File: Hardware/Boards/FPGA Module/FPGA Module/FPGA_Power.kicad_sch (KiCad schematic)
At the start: 41 parts, among them U1 XCKU3P-FFVA676

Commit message: Added NC to unused pins
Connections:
- no-connect marks 0 -> 1
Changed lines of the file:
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@@
 		(color 0 0 0 0)
 	)
+	(no_connect
+		(at 373.38 228.6)
+	)
 	(wire
 		(pts
@@
 	(wire
 		(pts
-			(xy 220.98 96.52) (xy 224.79 96.52)
-		)
-		(stroke
-			(width 0)
-			(type default)
-		)
-	)
-	(wire
-		(pts
 			(xy 374.65 175.26) (xy 373.38 175.26)
 		)
@@
 	(wire
 		(pts
+			(xy 220.98 109.22) (xy 224.79 109.22)
+		)
+		(stroke
+			(width 0)
+			(type default)
+		)
+	)
+	(wire
+		(pts
 			(xy 354.33 228.6) (xy 354.33 234.95)
 		)
@@
 	(wire
 		(pts
+			(xy 220.98 96.52) (xy 224.79 96.52)
+		)
+		(stroke
+			(width 0)
+			(type default)
+		)
+	)
+	(wire
+		(pts
 			(xy 212.09 134.62) (xy 213.36 134.62)
 		)
@@
 		)
 		(stroke
-			(width 0)
-			(type default)
-		)
-	)
-	(wire
-		(pts
-			(xy 220.98 109.22) (xy 224.79 109.22)
-		)
-		(stroke

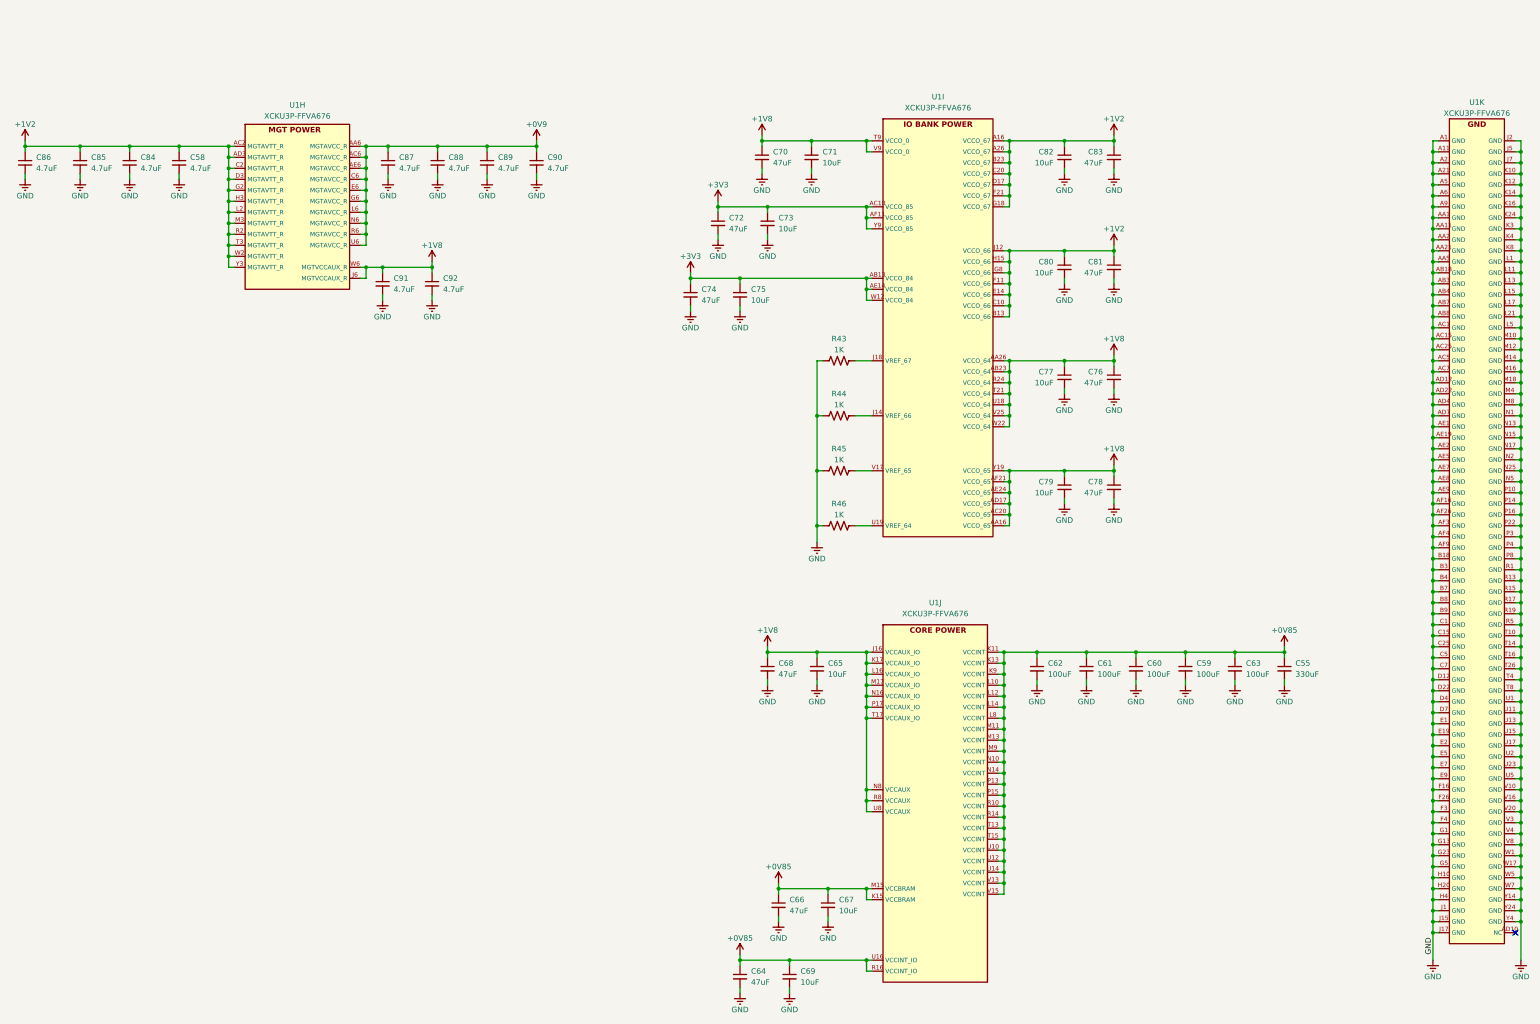
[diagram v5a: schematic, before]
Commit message: Completed FPGA module PCB layout
Started PCB routing
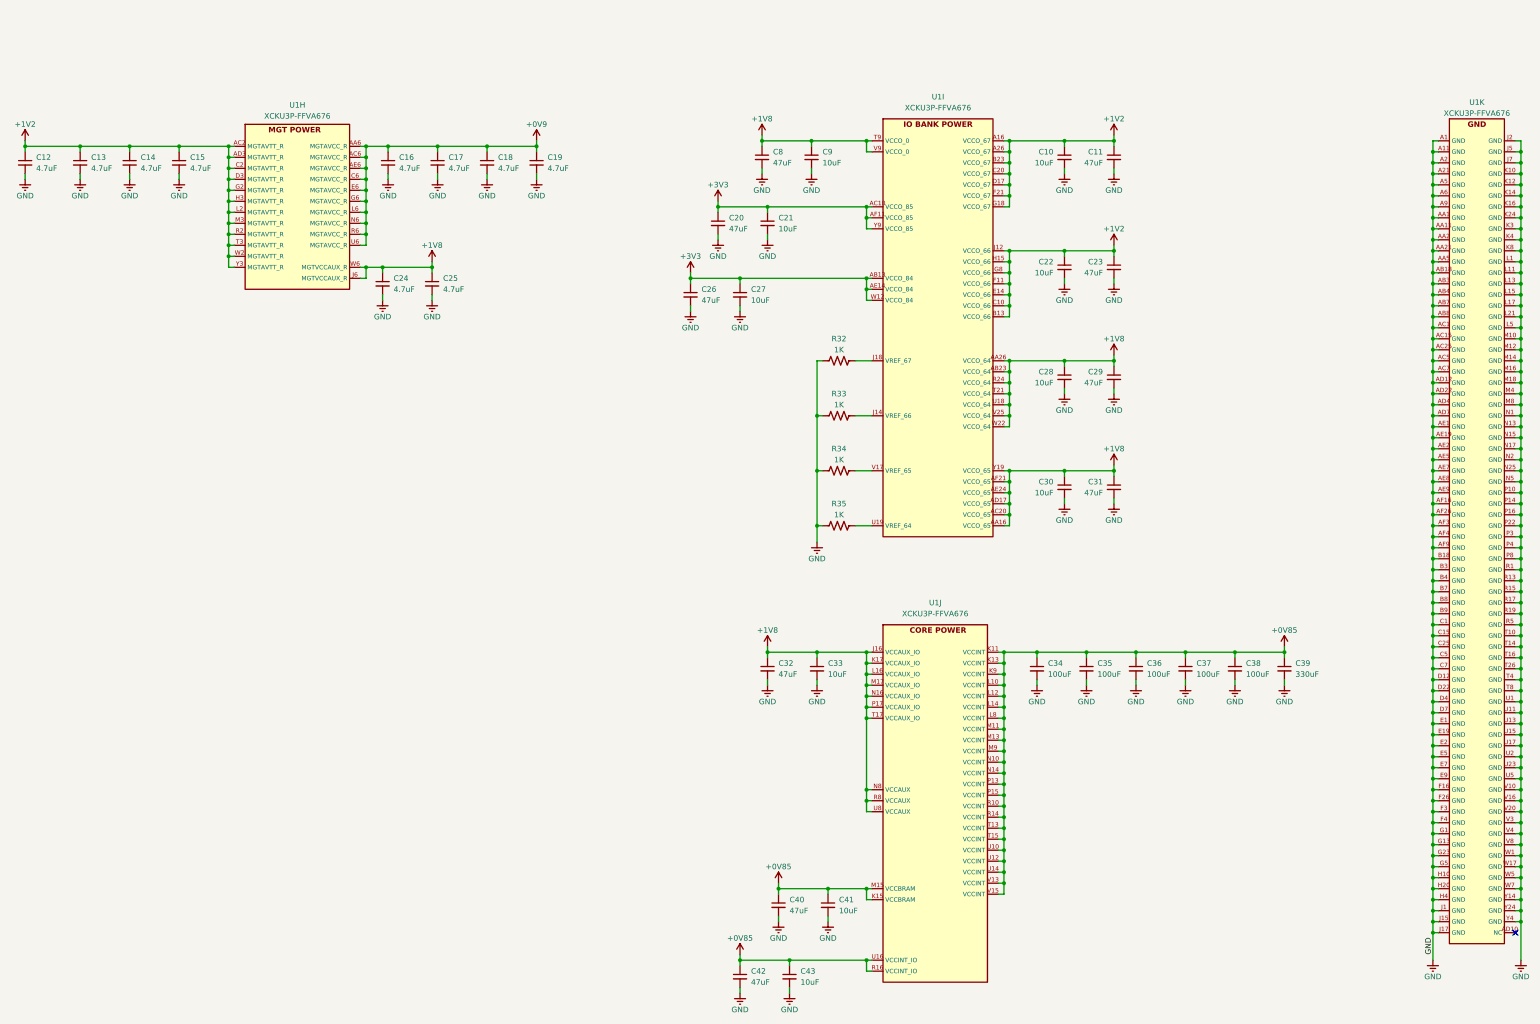
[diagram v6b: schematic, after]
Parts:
- removed C76, C83: 47uF, Capacitor_SMD:C_0603_1608Metric, symbol Device:C_Small
- removed C77, C82: 10uF, Capacitor_SMD:C_0402_1005Metric, symbol Device:C_Small
- added C10, C28: 10uF, Capacitor_SMD:C_0402_1005Metric, symbol Device:C_Small
- added C11, C29: 47uF, Capacitor_SMD:C_0603_1608Metric, symbol Device:C_Small
- R32: renamed from R43; footprint Resistor_SMD:R_0402_1005Metric -> Resistor_SMD:R_0201_0603Metric
- R33: renamed from R44; footprint Resistor_SMD:R_0402_1005Metric -> Resistor_SMD:R_0201_0603Metric
- R34: renamed from R45; footprint Resistor_SMD:R_0402_1005Metric -> Resistor_SMD:R_0201_0603Metric
- R35: renamed from R46; footprint Resistor_SMD:R_0402_1005Metric -> Resistor_SMD:R_0201_0603Metric
- renumbered C86 to C12, C85 to C13, C84 to C14, C58 to C15, C87 to C16, C88 to C17, C89 to C18, C90 to C19, C72 to C20, C73 to C21, C80 to C22, C81 to C23, C91 to C24, C92 to C25, C74 to C26, C75 to C27, C79 to C30, C78 to C31, C68 to C32, C65 to C33, C62 to C34, C61 to C35, C60 to C36, C59 to C37, C63 to C38, C55 to C39, C66 to C40, C67 to C41, C64 to C42, C69 to C43, C70 to C8, C71 to C9
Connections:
- net +1V2: now also C10.1, C11.1
- net +1V8: now also C28.1, C29.1
- net GND: now also C10.2, C11.2, C28.2, C29.2

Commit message: Updated SCH and Layout
Added temp sensors for DCDC's, Added MCU control for FPGA mode, removed mode DIP switch
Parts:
- C12, C13, C14, C15, C16, C17, C18, C19, C24, C25: footprint Capacitor_SMD:C_0402_1005Metric -> Capacitor_SMD:C_0201_0603Metric
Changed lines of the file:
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@@
 			)
 		)
-		(property "Footprint" "Capacitor_SMD:C_0402_1005Metric"
+		(property "Footprint" "Capacitor_SMD:C_0201_0603Metric"
 			(at 41.91 50.8 0)
 			(effects
@@
 			)
 		)
-		(property "Footprint" "Capacitor_SMD:C_0402_1005Metric"
+		(property "Footprint" "Capacitor_SMD:C_0201_0603Metric"
 			(at 123.19 78.74 0)
 			(effects
@@
 			)
 		)
-		(property "Footprint" "Capacitor_SMD:C_0402_1005Metric"
+		(property "Footprint" "Capacitor_SMD:C_0201_0603Metric"
 			(at 135.89 50.8 0)
 			(effects
@@
 			)
 		)
-		(property "Footprint" "Capacitor_SMD:C_0402_1005Metric"
+		(property "Footprint" "Capacitor_SMD:C_0201_0603Metric"
 			(at 53.34 50.8 0)
 			(effects
@@
 			)
 		)
-		(property "Footprint" "Capacitor_SMD:C_0402_1005Metric"
+		(property "Footprint" "Capacitor_SMD:C_0201_0603Metric"
 			(at 64.77 50.8 0)
 			(effects
@@
 			)
 		)
-		(property "Footprint" "Capacitor_SMD:C_0402_1005Metric"
+		(property "Footprint" "Capacitor_SMD:C_0201_0603Metric"
 			(at 29.21 50.8 0)
 			(effects
@@
 			)
 		)
-		(property "Footprint" "Capacitor_SMD:C_0402_1005Metric"
+		(property "Footprint" "Capacitor_SMD:C_0201_0603Metric"
 			(at 113.03 50.8 0)
 			(effects
@@
 			)
 		)
-		(property "Footprint" "Capacitor_SMD:C_0402_1005Metric"
+		(property "Footprint" "Capacitor_SMD:C_0201_0603Metric"
 			(at 111.76 78.74 0)
 			(effects
@@
 			)
 		)
-		(property "Footprint" "Capacitor_SMD:C_0402_1005Metric"
+		(property "Footprint" "Capacitor_SMD:C_0201_0603Metric"
 			(at 124.46 50.8 0)
 			(effects
@@
 			)
 		)
-		(property "Footprint" "Capacitor_SMD:C_0402_1005Metric"
+		(property "Footprint" "Capacitor_SMD:C_0201_0603Metric"
 			(at 147.32 50.8 0)
 			(effects
